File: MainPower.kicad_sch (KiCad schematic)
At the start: 76 parts, among them J11 Conn_01x02, J27 XT30PW-M, Q2 SQJ463EP-T1_GE3, U10 TPS2561, U3 TPS54561QDPRRQ1, U4 TPS54561QDPRRQ1, U5 LTC3622IDE-2-PBF

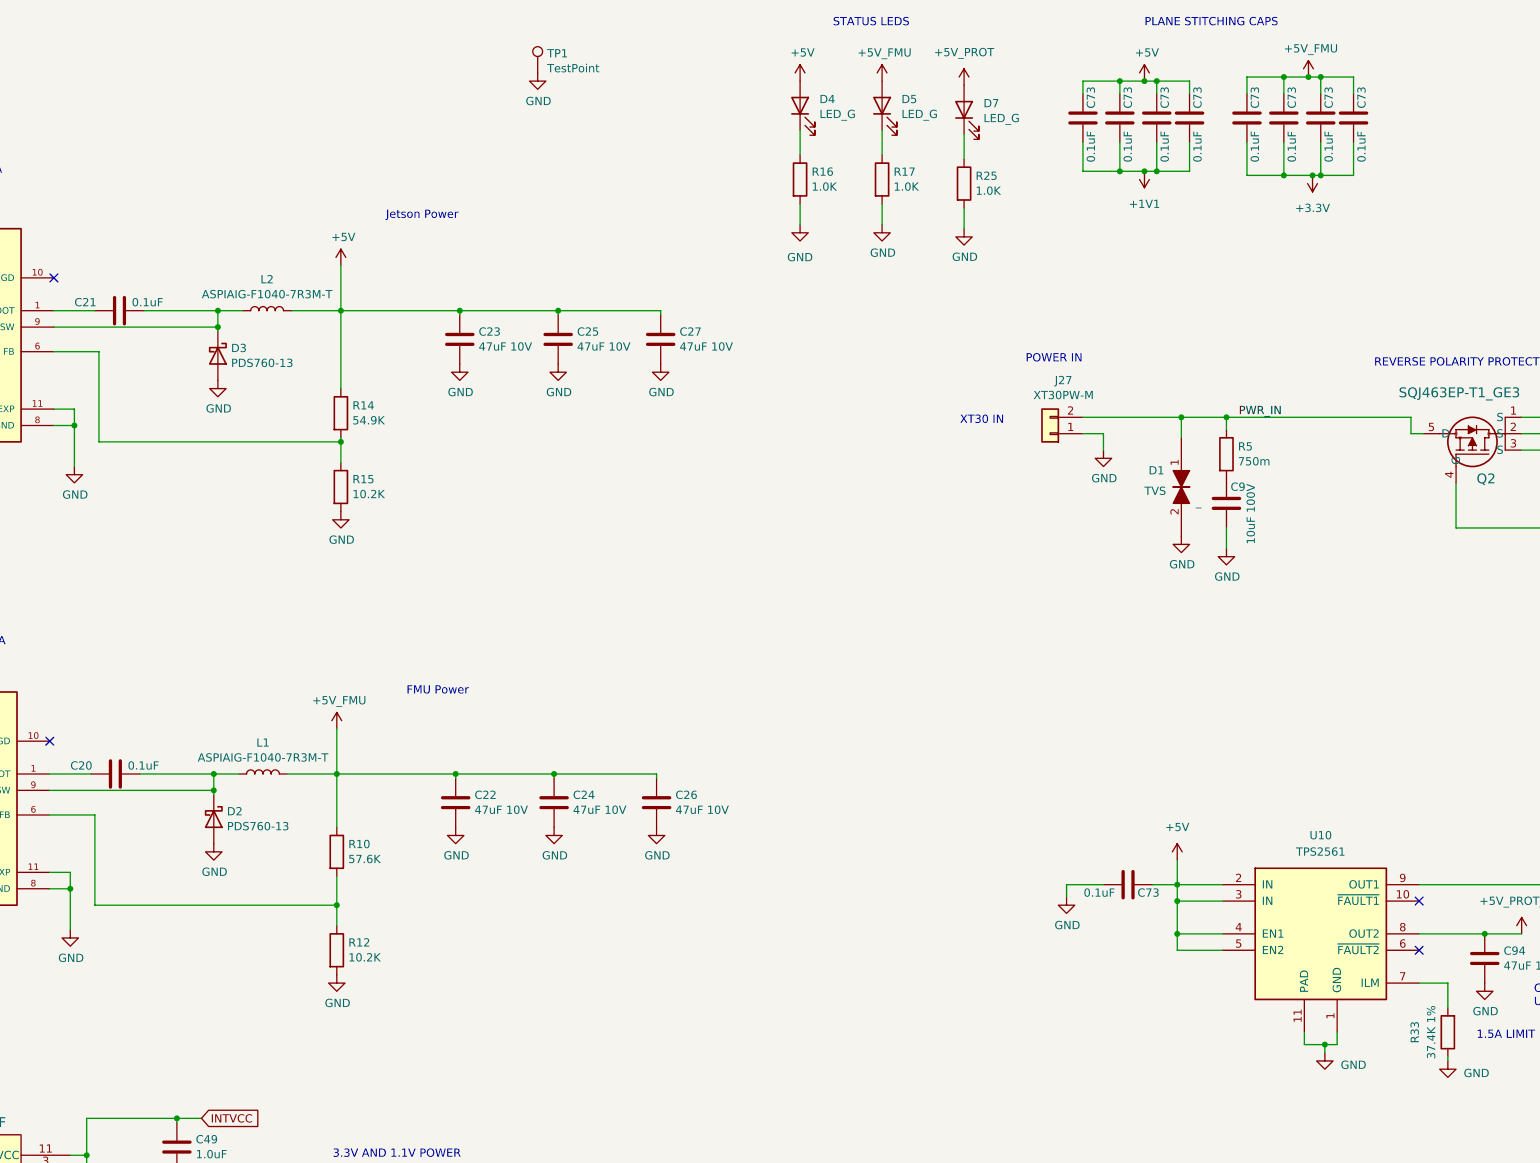
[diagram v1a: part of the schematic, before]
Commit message: updates for Rev1B boards, pinout changes on J5 and J8
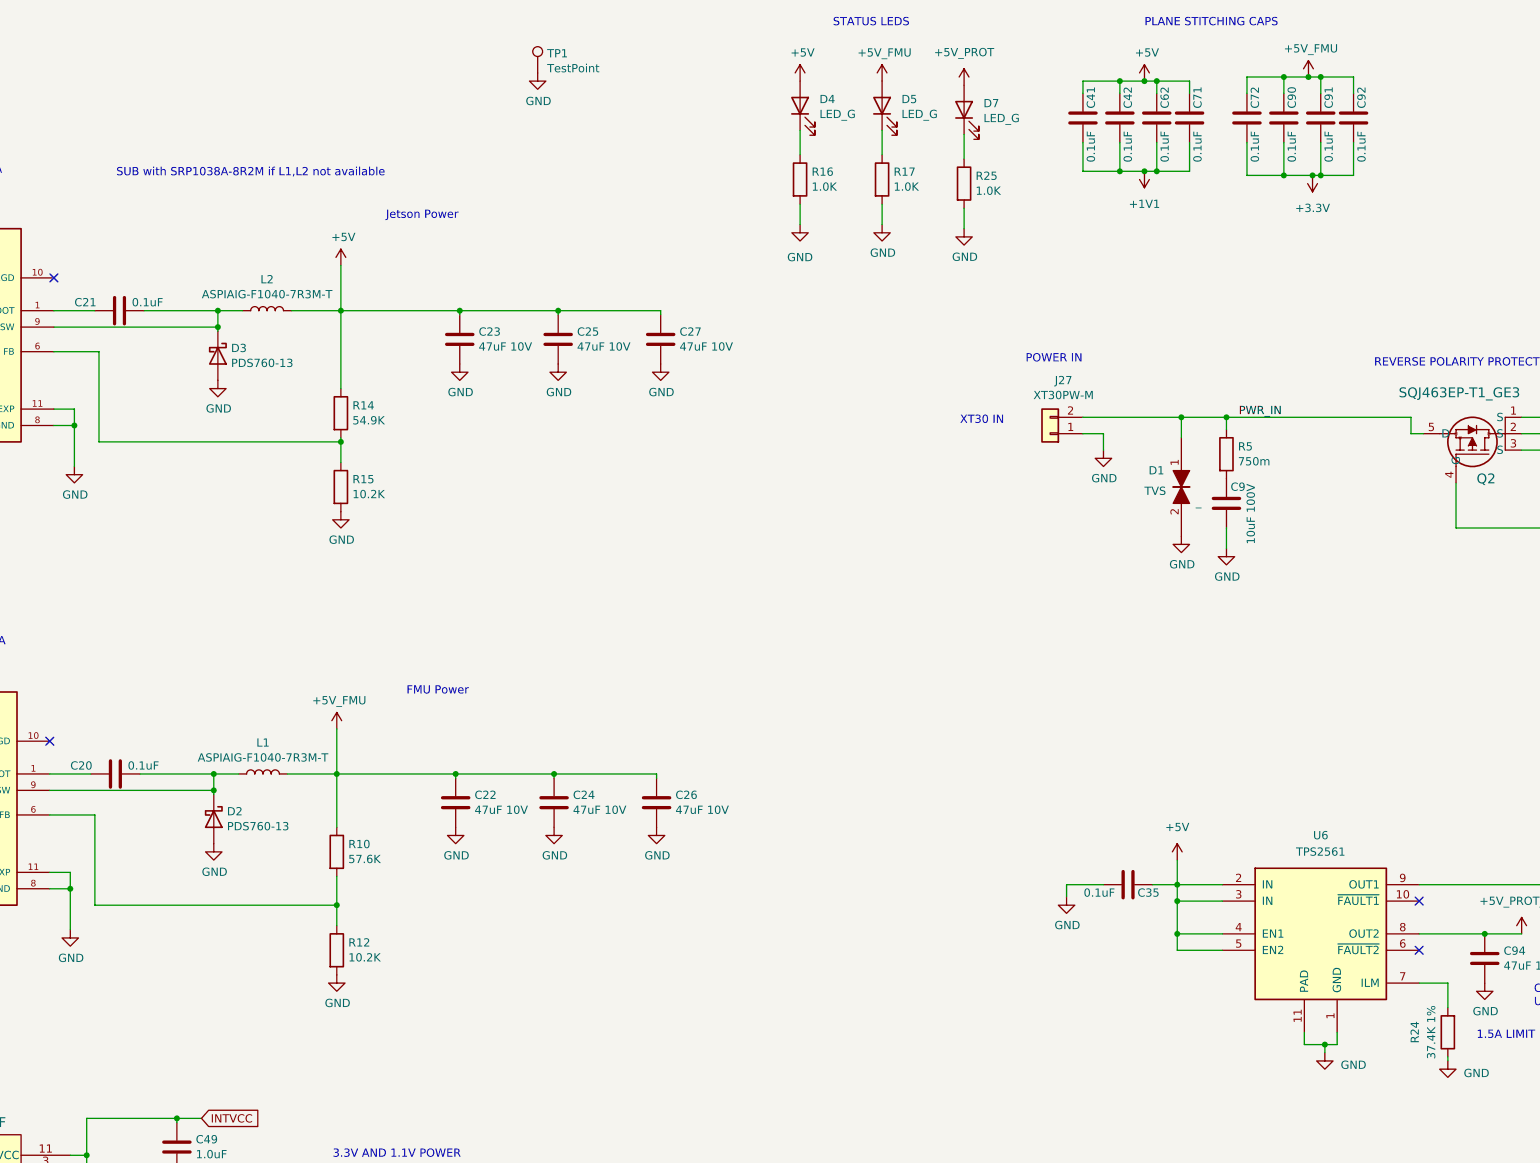
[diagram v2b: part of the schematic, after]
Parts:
- renumbered C73 to C35, C73 to C41, C73 to C42, C73 to C62, C73 to C71, C73 to C72, C73 to C90, C73 to C91, C73 to C92, R33 to R24, U10 to U6
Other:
- note added: "SUB with SRP1038A-8R2M if L1,L2 not available"
